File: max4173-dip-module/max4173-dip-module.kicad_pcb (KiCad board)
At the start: 2 copper layers, 7.6 x 10.2 mm, 5 parts, among them K1 CONN_3, K2 CONN_3, U1 MAX4173_SO8

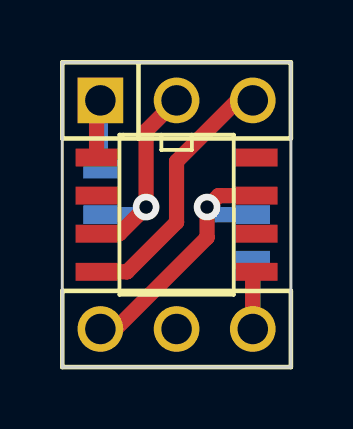
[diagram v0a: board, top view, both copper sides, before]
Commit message: embiggening a current-sense resistor pad
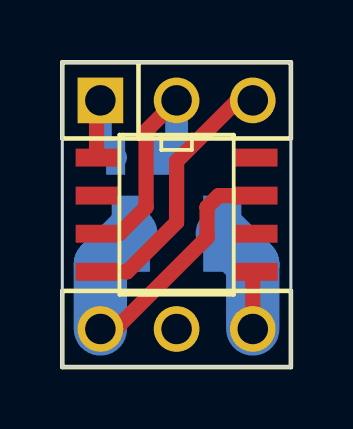
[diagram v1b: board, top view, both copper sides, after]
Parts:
- R1: footprint SM0603_Resistor -> SM1210
- moved R1 2.54 mm to (144.8, 67.9), turned to 0 degrees
- moved C1 1.71 mm to (143.5, 65.4), turned to 0 degrees
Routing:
- net /RS-: track 9.27 -> 11.2 mm, vias 1 -> 0
- net /RS+: track 4.24 -> 5.55 mm
- net /GND: track 7.63 -> 8.11 mm, vias 1 -> 0
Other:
- net class Default: trace_width 0.508 -> 0.762
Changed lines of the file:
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@@
   )
   (setup
-    (last_trace_width 0.508)
+    (last_trace_width 0.762)
     (trace_clearance 0.254)
     (zone_clearance 0.508)
@@
   (net_class Default "This is the default net class."
     (clearance 0.254)
-    (trace_width 0.508)
+    (trace_width 0.762)
     (via_dia 0.889)
     (via_drill 0.635)
@@
     )
   )
-  (module SM0603_Resistor (layer B.Cu)
-    (at 147.32 68.072 270)
+  (module SM0603_Capa (layer B.Cu)
+    (at 143.51 65.405)
     (attr smd)
-    (fp_text reference R1 (at 0.0635 0.0635 540) (layer B.SilkS)
-      (effects (font (size 0.50038 0.4572) (thickness 0.1143)) (justify mirror))
-    )
-    (fp_text value Rsense (at -1.69926 0 360) (layer B.SilkS) hide
+    (fp_text reference C1 (at 0 0 90) (layer B.SilkS)
       (effects (font (size 0.508 0.4572) (thickness 0.1143)) (justify mirror))
     )
-    (fp_line (start -0.50038 0.6985) (end -1.2065 0.6985) (layer B.SilkS) (width 0.127))
-    (fp_line (start -1.2065 0.6985) (end -1.2065 -0.6985) (layer B.SilkS) (width 0.127))
-    (fp_line (start -1.2065 -0.6985) (end -0.50038 -0.6985) (layer B.SilkS) (width 0.127))
-    (fp_line (start 1.2065 0.6985) (end 0.50038 0.6985) (layer B.SilkS) (width 0.127))
-    (fp_line (start 1.2065 0.6985) (end 1.2065 -0.6985) (layer B.SilkS) (width 0.127))
-    (fp_line (start 1.2065 -0.6985) (end 0.50038 -0.6985) (layer B.SilkS) (width 0.127))
-    (pad 1 smd rect (at -0.762 0 270) (size 0.635 1.143)
-      (layers B.Cu B.Paste B.Mask)
-      (net 4 /RS-)
-    )
-    (pad 2 smd rect (at 0.762 0 270) (size 0.635 1.143)
-      (layers B.Cu B.Paste B.Mask)
-      (net 3 /RS+)
-    )
-    (model smd\resistors\R0603.wrl
-      (at (xyz 0 0 0.001))
-      (scale (xyz 0.5 0.5 0.5))
-      (rotate (xyz 0 0 0))
-    )
-  )
-  (module SM0603_Capa (layer B.Cu)
-    (at 142.24 66.548 270)
-    (attr smd)
-    (fp_text reference C1 (at 0 0 540) (layer B.SilkS)
-      (effects (font (size 0.508 0.4572) (thickness 0.1143)) (justify mirror))
-    )
-    (fp_text value 0.1u (at -1.651 0 540) (layer B.SilkS)
+    (fp_text value 0.1u (at 0 0 90) (layer B.SilkS) hide
       (effects (font (size 0.508 0.4572) (thickness 0.1143)) (justify mirror))
     )
@@
     (fp_line (start 1.19888 0.635) (end 1.19888 -0.635) (layer B.SilkS) (width 0.11938))
     (fp_line (start -1.19888 -0.635) (end -1.19888 0.635) (layer B.SilkS) (width 0.11938))
-    (pad 1 smd rect (at -0.762 0 270) (size 0.635 1.143)
+    (pad 1 smd rect (at -0.762 0) (size 0.635 1.143)
       (layers B.Cu B.Paste B.Mask)
       (net 5 /Vcc)
     )
-    (pad 2 smd rect (at 0.762 0 270) (size 0.635 1.143)
+    (pad 2 smd rect (at 0.762 0) (size 0.635 1.143)
       (layers B.Cu B.Paste B.Mask)
       (net 1 /GND)
@@
       (at (xyz 0 0 0.001))
       (scale (xyz 0.5 0.5 0.5))
+      (rotate (xyz 0 0 0))
+    )
+  )
+  (module SM1210 (layer B.Cu)
+    (at 144.78 67.945)
+    (tags "CMS SM")
+    (attr smd)
+    (fp_text reference R1 (at 0 0 90) (layer B.SilkS)
+      (effects (font (size 0.762 0.762) (thickness 0.127)) (justify mirror))
+    )
+    (fp_text value Rsense (at 0 -0.508) (layer B.SilkS) hide
+      (effects (font (size 0.762 0.762) (thickness 0.127)) (justify mirror))
+    )
+    (fp_circle (center -2.413 -1.524) (end -2.286 -1.397) (layer B.SilkS) (width 0.127))
+    (fp_line (start -0.762 1.397) (end -2.286 1.397) (layer B.SilkS) (width 0.127))
+    (fp_line (start -2.286 1.397) (end -2.286 -1.397) (layer B.SilkS) (width 0.127))
+    (fp_line (start -2.286 -1.397) (end -0.762 -1.397) (layer B.SilkS) (width 0.127))
+    (fp_line (start 0.762 -1.397) (end 2.286 -1.397) (layer B.SilkS) (width 0.127))
+    (fp_line (start 2.286 -1.397) (end 2.286 1.397) (layer B.SilkS) (width 0.127))
+    (fp_line (start 2.286 1.397) (end 0.762 1.397) (layer B.SilkS) (width 0.127))
+    (pad 1 smd rect (at -1.524 0) (size 1.27 2.54)
+      (layers B.Cu B.Paste B.Mask)
+      (net 4 /RS-)
+    )
+    (pad 2 smd rect (at 1.524 0) (size 1.27 2.54)
+      (layers B.Cu B.Paste B.Mask)
+      (net 3 /RS+)
+    )
+    (model smd/chip_cms.wrl
+      (at (xyz 0 0 0))
+      (scale (xyz 0.17 0.2 0.17))
       (rotate (xyz 0 0 0))
     )
@@
   (gr_line (start 148.59 62.23) (end 148.59 72.39) (angle 90) (layer Edge.Cuts) (width 0.1))
   (gr_line (start 140.97 62.23) (end 148.59 62.23) (angle 90) (layer Edge.Cuts) (width 0.1))
-  (segment (start 142.24 67.31) (end 143.51 67.31) (width 0.508) (layer B.Cu) (net 1))
-  (via (at 143.764 67.056) (size 0.889) (layers F.Cu B.Cu) (net 1))
-  (segment (start 143.51 67.31) (end 143.764 67.056) (width 0.508) (layer B.Cu) (net 1))
+  (segment (start 144.78 63.5) (end 144.78 64.897) (width 0.762) (layer B.Cu) (net 1) (status 400000))
+  (segment (start 144.78 64.897) (end 144.272 65.405) (width 0.762) (layer B.Cu) (net 1) (status 800000))
   (segment (start 142.113 67.945) (end 142.875 67.945) (width 0.508) (layer F.Cu) (net 1))
   (segment (start 143.764 64.516) (end 144.78 63.5) (width 0.508) (layer F.Cu) (net 1))
@@
   (segment (start 144.78 67.564) (end 144.78 65.532) (width 0.508) (layer F.Cu) (net 2))
   (segment (start 143.129 69.215) (end 144.78 67.564) (width 0.508) (layer F.Cu) (net 2))
-  (segment (start 147.32 68.834) (end 147.32 71.12) (width 0.508) (layer B.Cu) (net 3))
+  (segment (start 147.32 71.12) (end 147.32 68.961) (width 1.778) (layer B.Cu) (net 3))
+  (segment (start 147.32 68.961) (end 146.304 67.945) (width 1.778) (layer B.Cu) (net 3))
   (segment (start 147.32 71.12) (end 147.32 69.342) (width 0.508) (layer F.Cu) (net 3))
   (segment (start 147.32 69.342) (end 147.447 69.215) (width 0.508) (layer F.Cu) (net 3))
-  (segment (start 147.32 67.31) (end 146.05 67.31) (width 0.508) (layer B.Cu) (net 4))
-  (via (at 145.796 67.056) (size 0.889) (layers F.Cu B.Cu) (net 4))
-  (segment (start 146.05 67.31) (end 145.796 67.056) (width 0.508) (layer B.Cu) (net 4))
+  (segment (start 142.24 71.12) (end 142.24 68.961) (width 1.778) (layer B.Cu) (net 4))
+  (segment (start 142.24 68.961) (end 143.256 67.945) (width 1.778) (layer B.Cu) (net 4))
   (segment (start 142.24 71.12) (end 142.748 71.12) (width 0.508) (layer F.Cu) (net 4))
   (segment (start 146.177 66.675) (end 147.447 66.675) (width 0.508) (layer F.Cu) (net 4))
@@
   (segment (start 145.796 68.072) (end 145.796 67.056) (width 0.508) (layer F.Cu) (net 4))
   (segment (start 142.748 71.12) (end 145.796 68.072) (width 0.508) (layer F.Cu) (net 4))
-  (segment (start 142.24 65.786) (end 142.24 63.5) (width 0.508) (layer B.Cu) (net 5))
+  (segment (start 142.24 63.5) (end 142.24 64.897) (width 0.762) (layer B.Cu) (net 5) (status 400000))
+  (segment (start 142.24 64.897) (end 142.748 65.405) (width 0.762) (layer B.Cu) (net 5) (status 800000))
   (segment (start 142.113 65.405) (end 142.113 63.627) (width 0.508) (layer F.Cu) (net 5))
   (segment (start 142.113 63.627) (end 142.24 63.5) (width 0.508) (layer F.Cu) (net 5))
